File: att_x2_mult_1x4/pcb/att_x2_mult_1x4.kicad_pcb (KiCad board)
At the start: 2 copper layers, 17.8 x 95.2 mm, 13 parts, among them J1 AudioJack2_SwitchT, J2 AudioJack2_SwitchT, J3 AudioJack2_SwitchT, J4 AudioJack2_SwitchT, J5 AudioJack2_SwitchT, J6 AudioJack2_SwitchT, J7 AudioJack2_SwitchT, J8 AudioJack2_SwitchT

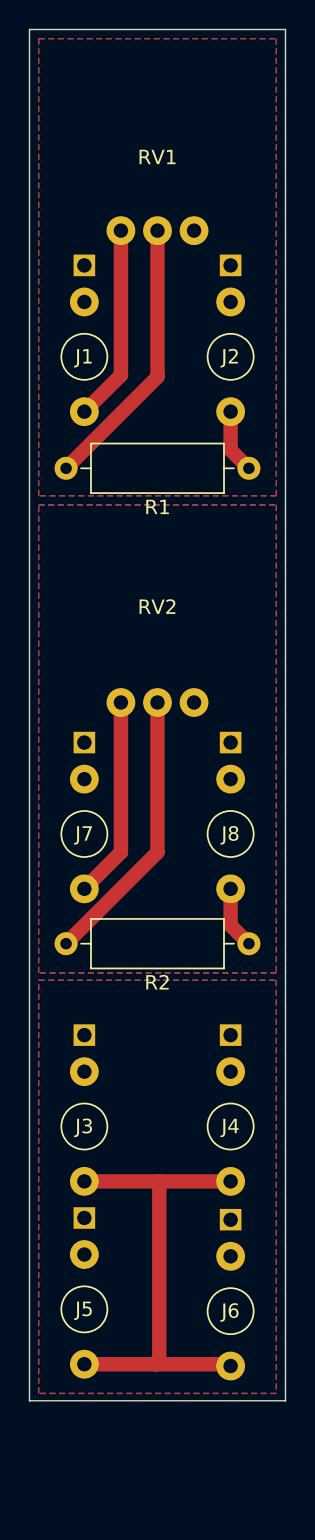
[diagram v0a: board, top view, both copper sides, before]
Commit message: extended mult to 2x3
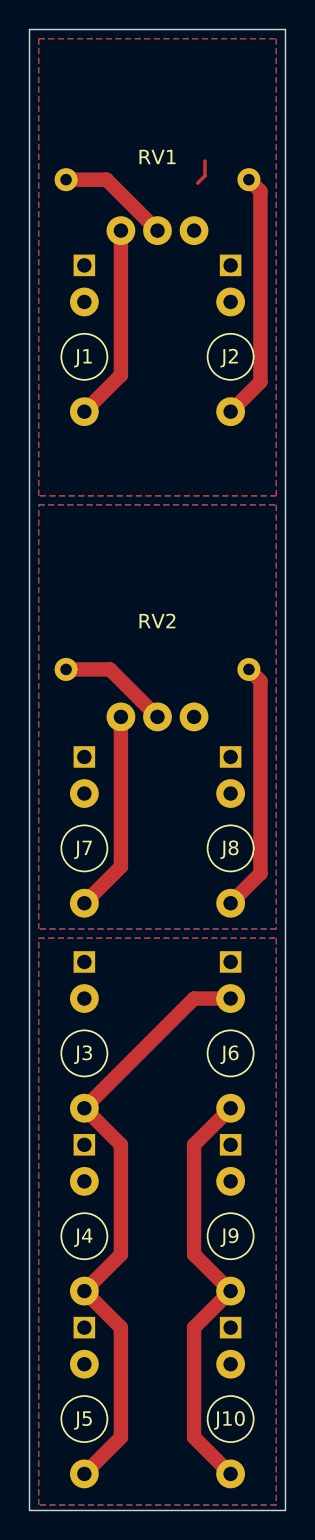
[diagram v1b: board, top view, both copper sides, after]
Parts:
- added J10: AudioJack2_SwitchT, eurorack_footprints:audio_jack_pj-398sm, F.Cu at (106.7, 175.3)
- added J9: AudioJack2_SwitchT, eurorack_footprints:audio_jack_pj-398sm, F.Cu at (106.7, 162.6)
- R1, R2: moved to B.Cu
- moved R1 20.0 mm to (108.0, 85.4)
- moved R2 19.1 mm to (108.0, 119.4)
- moved J6 17.9 mm to (106.7, 149.9)
- moved J4 12.7 mm to (96.5, 162.6)
- moved J5 7.62 mm to (96.5, 175.3)
- moved G*** 5.08 mm to (101.6, 146.1)
- moved J3 5.08 mm to (96.5, 149.9)
- moved J7 1.00 mm to (96.5, 135.6)
- moved J8 1.00 mm to (106.7, 135.6)
- moved RV2 1.00 mm to (99.1, 122.7)
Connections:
- J6 pad T: Net-(J3-PadT) -> Net-(J10-PadT)
- J6 pad TN: unconnected-(J6-PadTN) -> Net-(J3-PadT)
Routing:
- net Net-(J10-PadT): track 0.00 -> 29.6 mm
- net Net-(J8-PadT): track 4.34 -> 17.4 mm
- net Net-(J2-PadT): track 4.46 -> 17.3 mm
- net Net-(R2-Pad2): track 19.4 -> 7.72 mm
- net Net-(R1-Pad2): track 19.1 -> 7.82 mm
- net Net-(J3-PadT): track 33.2 -> 42.9 mm
- net (no net): track 0.00 -> 1.73 mm
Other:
- board size 17.8 x 95.2 mm -> 17.8 x 102.9 mm
- board text added: "MB20220614"
- board text removed: "MB20220612"

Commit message: revert cheanges on pat
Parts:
- removed J10, J9: AudioJack2_SwitchT, eurorack_footprints:audio_jack_pj-398sm
- R1, R2: moved to F.Cu
- moved R1 20.0 mm to (108.0, 105.4)
- moved R2 19.1 mm to (108.0, 138.4)
- moved J6 17.9 mm to (106.7, 167.8)
- moved J4 12.7 mm to (106.7, 154.9)
- moved J5 7.62 mm to (96.5, 167.6)
- moved G*** 5.08 mm to (101.6, 151.1)
- moved J3 5.08 mm to (96.5, 154.9)
- moved J7 1.00 mm to (96.5, 134.6)
- moved J8 1.00 mm to (106.7, 134.6)
- moved RV2 1.00 mm to (99.1, 121.7)
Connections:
- J6 pad T: Net-(J10-PadT) -> Net-(J3-PadT)
- J6 pad TN: Net-(J3-PadT) -> unconnected-(J6-PadTN)
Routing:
- net Net-(J10-PadT): track 29.6 -> 0.00 mm
- net Net-(J8-PadT): track 17.4 -> 4.34 mm
- net Net-(J2-PadT): track 17.3 -> 4.46 mm
- net Net-(RV2-Pad2): track 7.72 -> 19.4 mm
- net Net-(RV1-Pad2): track 7.82 -> 19.1 mm
- net Net-(J3-PadT): track 42.9 -> 33.2 mm
- net (no net): track 1.73 -> 0.00 mm
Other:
- board size 17.8 x 102.9 mm -> 17.8 x 95.2 mm
- board text added: "MB20220612"
- board text removed: "MB20220614"
